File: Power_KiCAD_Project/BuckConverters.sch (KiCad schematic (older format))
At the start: 14 parts

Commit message: Part Naming Correction
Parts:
- U?: value LM2678SX-3.3/NOPB -> LM2678SX-5.0/NOPB; Digikey https://www.digikey.com/en/products/detail/texas-instruments/LM2678SX-3-3-NOPB/366920 -> https://www.digikey.com/en/products/detail/texas-instruments/LM2677SX-5-0-NOPB/366916
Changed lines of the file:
@@
 P 4900 2850
 F 0 "U?" H 4900 3317 50  0000 C CNN
-F 1 "LM2678SX-3.3/NOPB" H 4900 3226 50  0000 C CNN
+F 1 "LM2678SX-5.0/NOPB" H 4900 3226 50  0000 C CNN
 F 2 "Package_TO_SOT_SMD:TO-263-7_TabPin8" H 4950 2500 50  0001 L CIN
-F 3 "https://www.ti.com/general/docs/suppproductinfo.tsp?distId=10&gotoUrl=http%3A%2F%2Fwww.ti.com%2Flit%2Fgpn%2Flm2678" H 4900 2850 50  0001 C CNN
-F 4 "https://www.digikey.com/en/products/detail/texas-instruments/LM2678SX-3-3-NOPB/366920" H 4900 2850 50  0001 C CNN "Digikey"
+F 3 "https://www.ti.com/lit/ds/symlink/lm2677.pdf" H 4900 2850 50  0001 C CNN
+F 4 "https://www.digikey.com/en/products/detail/texas-instruments/LM2677SX-5-0-NOPB/366916" H 4900 2850 50  0001 C CNN "Digikey"
 F 5 "https://webench.ti.com/wb5/PartDesigner/quickview.jsp?base_pn=LM2678&origin=ODS&litsection=application" H 4900 2850 50  0001 C CNN "Designer"
 	1    4900 2850

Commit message: added components
added a few components and the correct numbers
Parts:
- removed D? (x2): SBRD10200TR, symbol Device:D_Schottky
- added D5, D6: SBRD10200TR, SBRD10200TR:DPAK228P1005X240-4N, symbol SBRD10200TR:SBRD10200TR
- C21, C22: renamed from C?; symbol 35SVPF82M:35SVPF82M -> Power_KiCAD_Project-rescue:35SVPF82M-35SVPF82M
- C27: renamed from C?; symbol 16SVP330M:16SVP330M -> Power_KiCAD_Project-rescue:16SVP330M-16SVP330M
- C28: renamed from C?; symbol 6SVPC330M:6SVPC330M -> Power_KiCAD_Project-rescue:6SVPC330M-6SVPC330M
- U5, U6: renamed from U?; symbol lm2672m-to-263:LM2672M-TO-263 -> Power_KiCAD_Project-rescue:LM2672M-TO-263-lm2672m-to-263
- gave numbers to parts that had none: 6
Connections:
- net labels added: ground
- net labels removed: GND
- wire segments 46 -> 50
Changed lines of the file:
@@
 $Descr A4 11693 8268
 encoding utf-8
-Sheet 12 12
+Sheet 6 12
 Title "Buck Converter Supply"
 Date "2021-11-29"
@@
 $EndDescr
 $Comp
-L lm2672m-to-263:LM2672M-TO-263 U?
+L Power_KiCAD_Project-rescue:LM2672M-TO-263-lm2672m-to-263 U6
 U 1 1 61A319C7
 P 4900 5200
-F 0 "U?" H 4900 5667 50  0000 C CNN
+F 0 "U6" H 4900 5667 50  0000 C CNN
 F 1 "LM2678SX-3.3/NOPB" H 4900 5576 50  0000 C CNN
 F 2 "Package_TO_SOT_SMD:TO-263-7_TabPin8" H 4950 4850 50  0001 L CIN
@@
 $EndComp
 $Comp
-L Device:C C?
+L Device:C C24
 U 1 1 61A53C7C
 P 4050 5400
-F 0 "C?" H 4200 5400 50  0000 L CNN
+F 0 "C24" H 4200 5400 50  0000 L CNN
 F 1 "C0805C104M5RACTU" V 3900 5000 50  0000 L CNN
 F 2 "Capacitor_SMD:C_0805_2012Metric" H 4088 5250 50  0001 C CNN
@@
 Designed with 3S - 5S lithium pack in mind\nV_IN: 9V - 21V\n\n5A Output
 $Comp
-L 35SVPF82M:35SVPF82M C?
+L Power_KiCAD_Project-rescue:35SVPF82M-35SVPF82M C22
 U 1 1 61A4499B
 P 3400 5250
-F 0 "C?" V 3550 5350 60  0000 L CNN
+F 0 "C22" V 3550 5350 60  0000 L CNN
 F 1 "35SVPF82M" H 3350 5100 60  0000 L CNN
 F 2 "35SVPF82M:35SVPF82M" H 3550 4890 60  0001 C CNN
@@
 	4050 5000 4400 5000
 $Comp
-L Device:C_Small C?
+L Device:C_Small C26
 U 1 1 61A48396
 P 5650 5300
-F 0 "C?" H 5742 5346 50  0000 L CNN
+F 0 "C26" H 5742 5346 50  0000 L CNN
 F 1 "CGA4C2C0G1H103J060AA" H 5700 5250 39  0000 L CNN
 F 2 "Capacitor_SMD:C_0805_2012Metric" H 5650 5300 50  0001 C CNN
@@
 $EndComp
 $Comp
-L pspice:INDUCTOR L?
+L pspice:INDUCTOR L2
 U 1 1 61A496D2
 P 6950 5400
-F 0 "L?" H 6950 5615 50  0000 C CNN
+F 0 "L2" H 6950 5615 50  0000 C CNN
 F 1 "SER2915L-103KL" H 6950 5524 50  0000 C CNN
 F 2 "SER2915L-153KL:SER2915L-153KL" H 6950 5400 50  0001 C CNN
@@
 $EndComp
 $Comp
-L 6SVPC330M:6SVPC330M C?
+L Power_KiCAD_Project-rescue:6SVPC330M-6SVPC330M C28
 U 1 1 61A467E9
 P 7400 5550
-F 0 "C?" V 7500 5750 60  0000 L CNN
+F 0 "C28" V 7500 5750 60  0000 L CNN
 F 1 "6SVPC330M" H 7300 5700 60  0000 L CNN
 F 2 "6SVPC330M:6SVPC330M" H 7550 5190 60  0001 C CNN
@@
 Wire Wire Line
 	7200 5400 7400 5400
-$Comp
-L Device:D_Schottky D?
-U 1 1 61A4C464
-P 6100 5700
-F 0 "D?" V 6054 5780 50  0000 L CNN
-F 1 "SBRD10200TR" H 5850 5600 50  0000 L CNN
-F 2 "" H 6100 5700 50  0001 C CNN
-F 3 "~" H 6100 5700 50  0001 C CNN
-	1    6100 5700
-	0    1    1    0
-$EndComp
-Wire Wire Line
-	6100 6000 6100 5850
-Wire Wire Line
-	6100 6000 7400 6000
-Wire Wire Line
-	6100 5550 6100 5400
-Wire Wire Line
-	6100 5400 6700 5400
+Wire Wire Line
+	6100 6000 6300 6000
 Wire Wire Line
 	7400 5850 7400 6000
@@
 Wire Wire Line
 	5400 5200 5650 5200
-Wire Wire Line
-	5650 5400 6100 5400
 Connection ~ 5650 5400
-Connection ~ 6100 5400
 Wire Wire Line
 	7400 5000 7400 5400
 Wire Wire Line
 	5400 5000 7400 5000
-Connection ~ 6100 6000
-$Comp
-L power:GND #PWR?
-U 1 1 61A58607
-P 4050 5800
-F 0 "#PWR?" H 4050 5550 50  0001 C CNN
-F 1 "GND" H 4055 5627 50  0000 C CNN
-F 2 "" H 4050 5800 50  0001 C CNN
-F 3 "" H 4050 5800 50  0001 C CNN
-	1    4050 5800
-	1    0    0    -1
-$EndComp
-$Comp
-L power:GND #PWR?
-U 1 1 61A58BE6
-P 6100 6000
-F 0 "#PWR?" H 6100 5750 50  0001 C CNN
-F 1 "GND" H 6105 5827 50  0000 C CNN
-F 2 "" H 6100 6000 50  0001 C CNN
-F 3 "" H 6100 6000 50  0001 C CNN
-	1    6100 6000
-	1    0    0    -1
-$EndComp
 NoConn ~ 4400 5400
 Wire Notes Line
@@
 3.3V Buck Converter
 $Comp
-L lm2672m-to-263:LM2672M-TO-263 U?
+L Power_KiCAD_Project-rescue:LM2672M-TO-263-lm2672m-to-263 U5
 U 1 1 61A7F0DE
 P 4900 2850
-F 0 "U?" H 4900 3317 50  0000 C CNN
+F 0 "U5" H 4900 3317 50  0000 C CNN
 F 1 "LM2678SX-5.0/NOPB" H 4900 3226 50  0000 C CNN
 F 2 "Package_TO_SOT_SMD:TO-263-7_TabPin8" H 4950 2500 50  0001 L CIN
@@
 $EndComp
 $Comp
-L Device:C C?
+L Device:C C23
 U 1 1 61A7F0E5
 P 4050 3050
-F 0 "C?" H 4200 3050 50  0000 L CNN
+F 0 "C23" H 4200 3050 50  0000 L CNN
 F 1 "C0805C104M5RACTU" V 3900 2650 50  0000 L CNN
 F 2 "Capacitor_SMD:C_0805_2012Metric" H 4088 2900 50  0001 C CNN
@@
 $EndComp
 Wire Wire Line
-	3400 2650 3400 2900
-Wire Wire Line
 	3400 3450 3400 3200
 Wire Wire Line
 	4900 3450 4900 3250
-Wire Wire Line
-	3400 2650 3250 2650
-Connection ~ 3400 2650
 Text HLabel 3250 2650 0    50   Input ~ 0
 V_IN
 $Comp
-L 35SVPF82M:35SVPF82M C?
+L Power_KiCAD_Project-rescue:35SVPF82M-35SVPF82M C21
 U 1 1 61A7F0F2
 P 3400 2900
-F 0 "C?" V 3550 3000 60  0000 L CNN
+F 0 "C21" V 3550 3000 60  0000 L CNN
 F 1 "35SVPF82M" H 3350 2750 60  0000 L CNN
 F 2 "35SVPF82M:35SVPF82M" H 3550 2540 60  0001 C CNN
@@
 	3400 3450 4050 3450
 Wire Wire Line
-	3400 2650 4050 2650
-Wire Wire Line
 	4050 3200 4050 3450
 Connection ~ 4050 3450
@@
 	4050 2650 4400 2650
 $Comp
-L Device:C_Small C?
+L Device:C_Small C25
 U 1 1 61A7F101
 P 5650 2950
-F 0 "C?" H 5742 2996 50  0000 L CNN
+F 0 "C25" H 5742 2996 50  0000 L CNN
 F 1 "CGA4C2C0G1H103J060AA" H 5700 2900 39  0000 L CNN
 F 2 "Capacitor_SMD:C_0805_2012Metric" H 5650 2950 50  0001 C CNN
@@
 $EndComp
 $Comp
-L pspice:INDUCTOR L?
+L pspice:INDUCTOR L1
 U 1 1 61A7F108
 P 6950 3050
-F 0 "L?" H 6950 3265 50  0000 C CNN
+F 0 "L1" H 6950 3265 50  0000 C CNN
 F 1 "MSS1210-153MEB" H 6950 3174 50  0000 C CNN
 F 2 "MSS1210-153MEB:INDPM120120X1020N" H 6950 3050 50  0001 C CNN
@@
 Wire Wire Line
 	7200 3050 7400 3050
-$Comp
-L Device:D_Schottky D?
-U 1 1 61A7F115
-P 6100 3350
-F 0 "D?" V 6054 3430 50  0000 L CNN
-F 1 "SBRD10200TR" H 5850 3250 50  0000 L CNN
-F 2 "" H 6100 3350 50  0001 C CNN
-F 3 "~" H 6100 3350 50  0001 C CNN
-	1    6100 3350
-	0    1    1    0
-$EndComp
-Wire Wire Line
-	6100 3650 6100 3500
-Wire Wire Line
-	6100 3650 7400 3650
 Wire Wire Line
 	6100 3200 6100 3050
@@
 Wire Wire Line
 	5400 2650 7400 2650
-Connection ~ 6100 3650
-$Comp
-L power:GND #PWR?
-U 1 1 61A7F12C
-P 4050 3450
-F 0 "#PWR?" H 4050 3200 50  0001 C CNN
-F 1 "GND" H 4055 3277 50  0000 C CNN
-F 2 "" H 4050 3450 50  0001 C CNN
-F 3 "" H 4050 3450 50  0001 C CNN
-	1    4050 3450
-	1    0    0    -1
-$EndComp
-$Comp
-L power:GND #PWR?
-U 1 1 61A7F132
-P 6100 3650
-F 0 "#PWR?" H 6100 3400 50  0001 C CNN
-F 1 "GND" H 6105 3477 50  0000 C CNN
-F 2 "" H 6100 3650 50  0001 C CNN
-F 3 "" H 6100 3650 50  0001 C CNN
-	1    6100 3650
-	1    0    0    -1
-$EndComp
 NoConn ~ 4400 3050
 Wire Notes Line
@@
 5V Buck Converter
 $Comp
-L 16SVP330M:16SVP330M C?
+L Power_KiCAD_Project-rescue:16SVP330M-16SVP330M C?
 U 1 1 61A47D3A
 P 7400 3200
-F 0 "C?" V 7497 3305 60  0000 L CNN
+AR Path="/61A47D3A" Ref="C?"  Part="1"
+AR Path="/61A48488/61A47D3A" Ref="C27"  Part="1"
+F 0 "C27" V 7497 3305 60  0000 L CNN
 F 1 "16SVP330M" V 7603 3305 60  0000 L CNN
 F 2 "PCAP_SVP_F12_PAN" H 7550 2840 60  0001 C CNN
@@
 Wire Wire Line
 	3400 5800 3400 5550
+Text HLabel 4050 3450 3    50   Input ~ 0
+ground
+Text HLabel 6000 3650 0    50   Input ~ 0
+ground
+Text HLabel 6100 6000 0    50   Input ~ 0
+ground
+Text HLabel 4050 5800 3    50   Input ~ 0
+ground
+$Comp
+L SBRD10200TR:SBRD10200TR D5
+U 1 1 61A8FF3C
+P 6100 3400
+F 0 "D5" H 6276 3441 50  0000 L CNN
+F 1 "SBRD10200TR" H 6276 3350 50  0000 L CNN
+F 2 "SBRD10200TR:DPAK228P1005X240-4N" H 6100 3400 50  0001 L BNN
+F 3 "" H 6100 3400 50  0001 L BNN
+F 4 "SBRD10200TR" H 6100 3400 50  0001 L BNN "MP"
+F 5 "1655-1939-1-ND" H 6100 3400 50  0001 L BNN "Digi-Key_Part_Number"
+F 6 "TO-252-3 SMC" H 6100 3400 50  0001 L BNN "Package"
+F 7 "Diode Schottky 200 V 10A Surface Mount DPAK" H 6100 3400 50  0001 L BNN "Description"
+F 8 "SMC Diode" H 6100 3400 50  0001 L BNN "MF"
+	1    6100 3400
+	1    0    0    -1
+$EndComp
+$Comp
+L SBRD10200TR:SBRD10200TR D6
+U 1 1 61A94D59
+P 6200 5600
+F 0 "D6" H 6376 5641 50  0000 L CNN
+F 1 "SBRD10200TR" H 6376 5550 50  0000 L CNN
+F 2 "SBRD10200TR:DPAK228P1005X240-4N" H 6200 5600 50  0001 L BNN
+F 3 "" H 6200 5600 50  0001 L BNN
+F 4 "SBRD10200TR" H 6200 5600 50  0001 L BNN "MP"
+F 5 "1655-1939-1-ND" H 6200 5600 50  0001 L BNN "Digi-Key_Part_Number"
+F 6 "TO-252-3 SMC" H 6200 5600 50  0001 L BNN "Package"
+F 7 "Diode Schottky 200 V 10A Surface Mount DPAK" H 6200 5600 50  0001 L BNN "Description"
+F 8 "SMC Diode" H 6200 5600 50  0001 L BNN "MF"
+	1    6200 5600
+	1    0    0    -1
+$EndComp
+Wire Wire Line
+	5650 5400 6200 5400
+Connection ~ 6200 5400
+Wire Wire Line
+	6200 5400 6700 5400
+Wire Wire Line
+	6300 5800 6300 6000
+Connection ~ 6300 6000
+Wire Wire Line
+	6300 6000 7400 6000
+Wire Wire Line
+	6100 5800 6100 6000
+Wire Wire Line
+	6000 3650 6200 3650
+Wire Wire Line
+	6000 3600 6000 3610
+Connection ~ 6000 3610
+Wire Wire Line
+	6000 3610 6000 3650
+Wire Wire Line
+	6200 3600 6200 3650
+Connection ~ 6200 3650
+Wire Wire Line
+	6200 3650 7400 3650
+Wire Wire Line
+	3250 2650 3400 2650
+Wire Wire Line
+	3400 2900 3400 2650
+Connection ~ 3400 2650
+Wire Wire Line
+	3400 2650 4050 2650
 $EndSCHEMATC

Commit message: pcb finished
pcb is done. 3am kicad be like
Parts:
- removed C21, C22: 35SVPF82M, 35SVPF82M:35SVPF82M, symbol Power_KiCAD_Project-rescue:35SVPF82M-35SVPF82M
- removed C23, C24: C0805C104M5RACTU, Capacitor_SMD:C_0805_2012Metric, symbol Device:C
- removed C25, C26: CGA4C2C0G1H103J060AA, Capacitor_SMD:C_0805_2012Metric, symbol Device:C_Small
- removed C27: 16SVP330M, PCAP_SVP_F12_PAN, symbol Power_KiCAD_Project-rescue:16SVP330M-16SVP330M
- removed C28: 6SVPC330M, 6SVPC330M:6SVPC330M, symbol Power_KiCAD_Project-rescue:6SVPC330M-6SVPC330M
- removed L1: MSS1210-153MEB, MSS1210-153MEB:INDPM120120X1020N, symbol pspice:INDUCTOR
- removed L2: SER2915L-103KL, SER2915L-153KL:SER2915L-153KL, symbol pspice:INDUCTOR
- added C21, C22: 35SVPF82M, SamacSys_Parts:16SVPT560M, symbol SamacSys_Parts:35SVPF82M
- added C23, C24: C0805C104M5RACTU, SamacSys_Parts:CAPC2012X88N, symbol SamacSys_Parts:C0805C104M5RACTU
- added C25, C26: CGA4C2C0G1H103J060AA, SamacSys_Parts:CAPC2012X75N, symbol SamacSys_Parts:CGA4C2C0G1H103J060AA
- added C27: 16SVP330M, SamacSys_Parts:16SVF1000M, symbol SamacSys_Parts:16SVP330M
- added C28: 6SVPC330M, SamacSys_Parts:16SVF180M, symbol SamacSys_Parts:6SVPC330M
- added L1: SRP1270-8R2M, SamacSys_Parts:INDPM137129X700N, symbol SamacSys_Parts:SRP1270-8R2M
- added L2: MSS1210-153MEB, MSS1210-153MEB:IND_MSS1210-153MEB, symbol MSS1210-153MEB:MSS1210-153MEB
- renumbered U5 to U4, U6 to U5
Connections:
- wire segments 50 -> 61

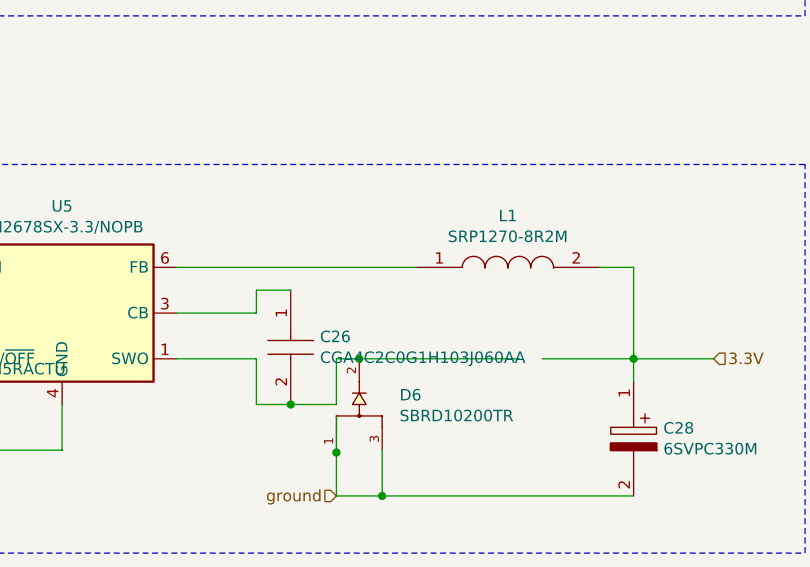
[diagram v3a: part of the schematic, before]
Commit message: updated pcb
more updates because stuff was a bit too far away from their connected components
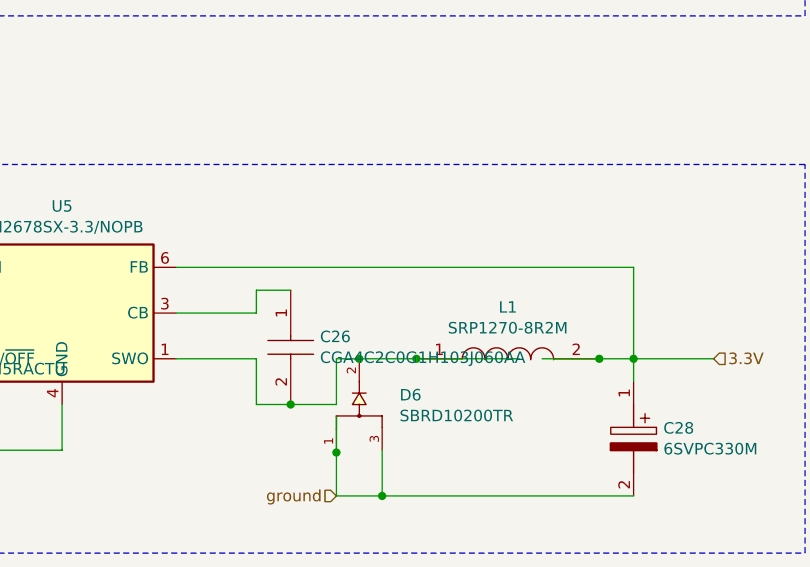
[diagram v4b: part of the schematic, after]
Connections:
- wire segments 61 -> 62
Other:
- moved on the sheet: L1
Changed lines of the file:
@@
 	5400 5200 5750 5200
 Wire Wire Line
-	6200 5400 6900 5400
+	6200 5400 6450 5400
 Wire Wire Line
-	7000 5400 7400 5400
+	7000 5400 7250 5400
 $Comp
 L Power_KiCAD_Project-rescue:LM2672M-TO-263-lm2672m-to-263 U4
@@
 L SamacSys_Parts:SRP1270-8R2M L1
 U 1 1 61D4AE9F
-P 6450 5000
-F 0 "L1" H 6850 5225 50  0000 C CNN
-F 1 "SRP1270-8R2M" H 6850 5134 50  0000 C CNN
-F 2 "SamacSys_Parts:INDPM137129X700N" H 7100 5050 50  0001 L CNN
-F 3 "https://datasheet.datasheetarchive.com/originals/distributors/SFDatasheet-7/sf-000140448.pdf" H 7100 4950 50  0001 L CNN
-F 4 "Bourns, SRP1270, 1270 Shielded Wire-wound SMD Inductor with a Iron Core, 8.2 uH +/-20% Wire-Wound 17A Idc" H 7100 4850 50  0001 L CNN "Description"
-F 5 "7" H 7100 4750 50  0001 L CNN "Height"
-F 6 "652-SRP1270-8R2M" H 7100 4650 50  0001 L CNN "Mouser Part Number"
-F 7 "https://www.mouser.co.uk/ProductDetail/Bourns/SRP1270-8R2M?qs=s%252BX%2FYkvGCpF9VN%2FUv1apFg%3D%3D" H 7100 4550 50  0001 L CNN "Mouser Price/Stock"
-F 8 "Bourns" H 7100 4450 50  0001 L CNN "Manufacturer_Name"
-F 9 "SRP1270-8R2M" H 7100 4350 50  0001 L CNN "Manufacturer_Part_Number"
-	1    6450 5000
+P 6450 5400
+F 0 "L1" H 6850 5625 50  0000 C CNN
+F 1 "SRP1270-8R2M" H 6850 5534 50  0000 C CNN
+F 2 "SamacSys_Parts:INDPM137129X700N" H 7100 5450 50  0001 L CNN
+F 3 "https://datasheet.datasheetarchive.com/originals/distributors/SFDatasheet-7/sf-000140448.pdf" H 7100 5350 50  0001 L CNN
+F 4 "Bourns, SRP1270, 1270 Shielded Wire-wound SMD Inductor with a Iron Core, 8.2 uH +/-20% Wire-Wound 17A Idc" H 7100 5250 50  0001 L CNN "Description"
+F 5 "7" H 7100 5150 50  0001 L CNN "Height"
+F 6 "652-SRP1270-8R2M" H 7100 5050 50  0001 L CNN "Mouser Part Number"
+F 7 "https://www.mouser.co.uk/ProductDetail/Bourns/SRP1270-8R2M?qs=s%252BX%2FYkvGCpF9VN%2FUv1apFg%3D%3D" H 7100 4950 50  0001 L CNN "Mouser Price/Stock"
+F 8 "Bourns" H 7100 4850 50  0001 L CNN "Manufacturer_Name"
+F 9 "SRP1270-8R2M" H 7100 4750 50  0001 L CNN "Manufacturer_Part_Number"
+	1    6450 5400
 	1    0    0    -1
 $EndComp
-Wire Wire Line
-	5400 5000 6450 5000
-Wire Wire Line
-	7250 5000 7400 5000
 Wire Wire Line
 	6100 5650 6100 5810
@@
 Wire Wire Line
 	6100 5810 6100 6000
+Connection ~ 6450 5400
+Wire Wire Line
+	6450 5400 6900 5400
+Connection ~ 7250 5400
+Wire Wire Line
+	7250 5400 7400 5400
+Wire Wire Line
+	5400 5000 7400 5000
 $EndSCHEMATC
